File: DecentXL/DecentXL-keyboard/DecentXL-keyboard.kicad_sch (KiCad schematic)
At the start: 206 parts, among them J1 Conn_02x12_Odd_Even, J2 Conn_01x26, J3 Conn_01x04, SW0 SW_Push_45deg, SW1 SW_Push_45deg, SW2 SW_Push_45deg, SW3 SW_Push_45deg, SW4 SW_Push_45deg, SW5 SW_Push_45deg, SW6 SW_Push_45deg, SW8 SW_Push_45deg, SW9 SW_Push_45deg

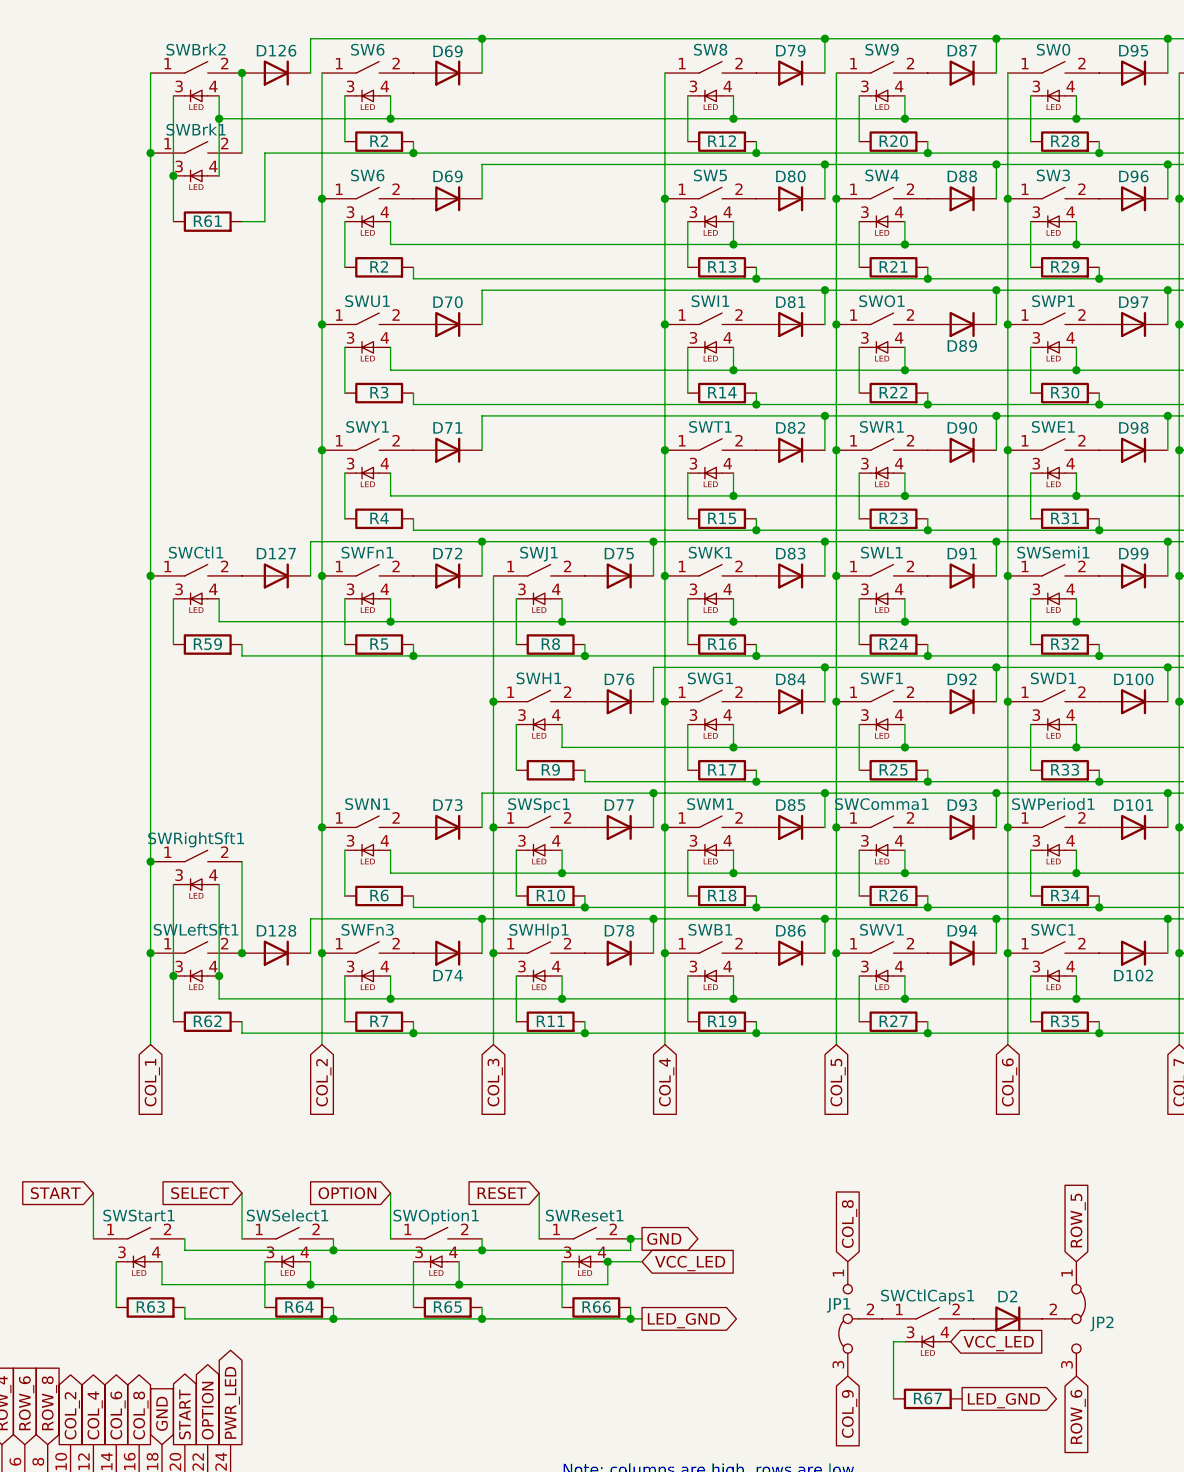
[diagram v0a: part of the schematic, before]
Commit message: DecentXL footprint library with Alps compatible footprint
Other usable footprints: MX, Kailh Choc v2
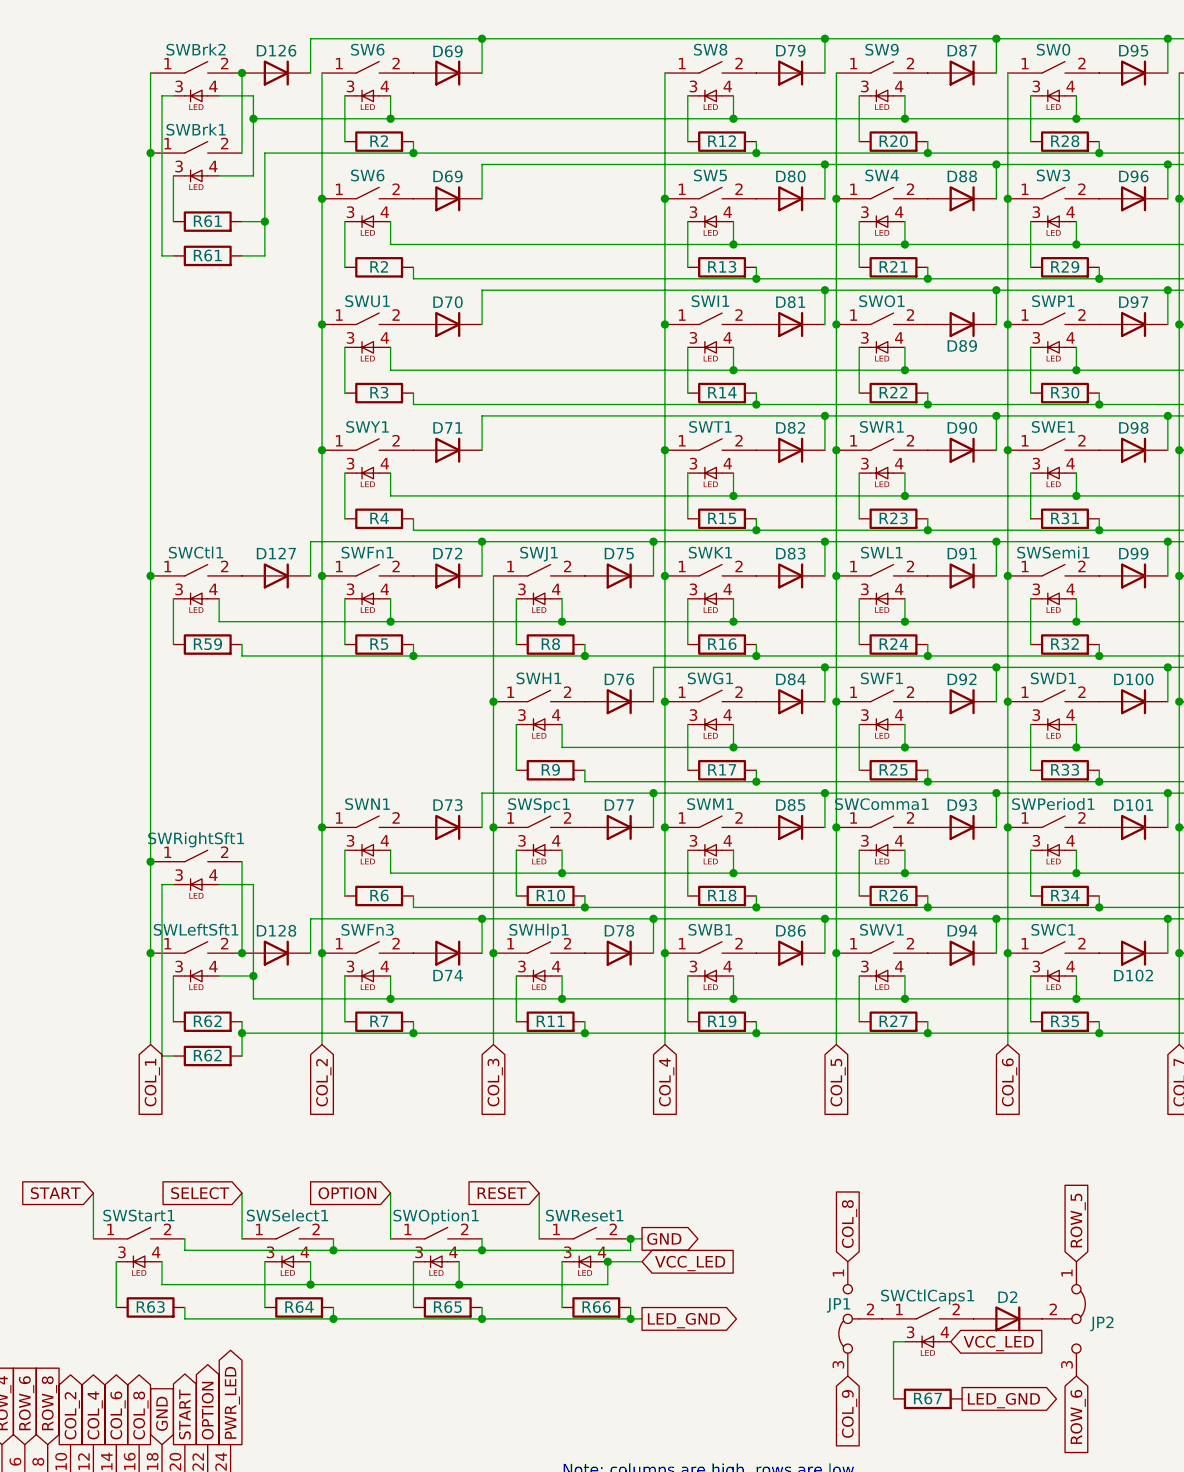
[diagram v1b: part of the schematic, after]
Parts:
- added R61, R62: R, Resistor_SMD:R_0603_1608Metric, symbol Device:R
- J1: footprint Atari130MX:IDC-Header_2x12_P2.54mm_Vertical -> Connector_IDC:IDC-Header_2x12_P2.54mm_Vertical
- SW0, SW1, SW2, SW3, SW4, SW5, SW6, SW8, SW9, SWA1, SWB1, SWBrk1, SWBrk2, SWC1, SWComma1, SWD1, SWDash1, SWDel1, SWE1, SWEqual1, SWEsc1, SWF1, SWG1, SWGT1, SWH1, SWI1, SWInv1, SWJ1, SWK1, SWL1, SWLT1, SWM1, SWN1, SWO1, SWP1, SWPeriod1, SWPlus1, SWQ1, SWR1, SWS1, SWSemi1, SWSlash1, SWStar1, SWT1, SWU1, SWV1, SWW1, SWX1, SWY1, SWZ1: footprint Atari130MX:MX-1U-LED -> DecentXL:MX-1-00U-LED
- SWCps1, SWCtl1: footprint Atari130MX:MX-1-25U-LED -> DecentXL:MX-1-25U-LED
- SWCtlCaps1, SWRightSft1: footprint Atari130MX:MX-1-75U-LED -> DecentXL:MX-1-75U-LED
- SWDel2: footprint Atari130MX:MX-2-00U -> DecentXL:MX-2-00U-LED
- SWFn1, SWFn2, SWFn3, SWFn4, SWHlp1, SWOption1, SWReset1, SWSelect1, SWStart1: footprint Atari130MX:MX-1-50U-Atari-Fn-LED -> DecentXL:MX-1-50U-Atari-Fn-LED
- SWLeftSft1: footprint Atari130MX:MX-2-25U-LED -> DecentXL:MX-2-25U-LED
- SWRet1, SWTab1: footprint Atari130MX:MX-1-50U-LED -> DecentXL:MX-1-50U-LED
- SWRet2: footprint Atari130MX:MX-ISO-RETURN -> DecentXL:MX-ISO-RETURN
- SWSpc1: footprint Atari130MX:MX-6-50U-LED -> DecentXL:MX-6-25U-LED
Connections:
- net LED_GND: now also R61.2, R62.2
- net at R62.1, SWLeftSft1.3: no longer SWRightSft1.3
- net at R61.1, SWBrk1.3: no longer SWBrk2.3
- new net: R62.1, SWRightSft1.3
- new net: R61.1, SWBrk2.3

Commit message: DecentXL PCB
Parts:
- added J4, J7: Conn_01x10, Connector_PinHeader_2.54mm:PinHeader_1x10_P2.54mm_Vertical, symbol Connector_Generic:Conn_01x10
- added J5, J6: Conn_01x10, Connector_FFC-FPC:TE_1-1734839-0_1x10-1MP_P0.5mm_Horizontal, symbol Connector_Generic:Conn_01x10
- D100, D101, D102, D103, D104, D105, D106, D107, D108, D109, D110, D111, D112, D113, D114, D115, D116, D117, D118, D119, D120, D121, D122, D123, D124, D125, D126, D127, D128, D2, D69, D70, D71, D72, D73, D74, D75, D76, D77, D78, D79, D80, D81, D82, D83, D84, D85, D86, D87, D88, D89, D90, D91, D92, D93, D94, D95, D96, D97, D98, D99: footprint Diode_SMD:D_SOD-123 -> DecentXL:D_SOD-123
- R10, R11, R12, R13, R14, R15, R16, R17, R18, R19, R2, R20, R21, R22, R23, R24, R25, R26, R27, R28, R29, R3, R30, R31, R32, R33, R34, R35, R36, R37, R38, R39, R4, R40, R41, R42, R43, R44, R45, R46, R47, R48, R49, R5, R50, R51, R52, R53, R54, R55, R56, R57, R58, R59, R6, R61, R62, R63, R64, R65, R66, R67, R7, R8, R9: footprint Resistor_SMD:R_0603_1608Metric -> DecentXL:R_0603_1608Metric
- SWBrk2: footprint DecentXL:MX-1-00U-LED -> DecentXL:MX-1-25U-LED
- SWFn1, SWFn2, SWFn3, SWFn4, SWHlp1, SWOption1, SWReset1, SWSelect1, SWStart1: footprint DecentXL:MX-1-50U-Atari-Fn-LED -> DecentXL:MX-1-00U-LED
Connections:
- net COL_1: now also JP1.3 (B)
- net COL_3: now also J6.9 (Pin_9), J7.9 (Pin_9); no longer SWHlp1.1
- net COL_8: no longer JP1.1 (A)
- net COL_9: now also JP1.1 (A); no longer JP1.3 (B)
- net GND: now also J6.8 (Pin_8), J7.8 (Pin_8); no longer D1.1 (K), SWOption1.2, SWReset1.2, SWSelect1.2, SWStart1.2
- net LED_GND: now also J6.1 (Pin_1), J7.1 (Pin_1); no longer R11.2, R63.2, R64.2, R65.2, R66.2
- net OPTION: now also J6.5 (Pin_5), J7.5 (Pin_5); no longer SWOption1.1
- net PWR_LED: now also J6.3 (Pin_3), J7.3 (Pin_3); no longer D1.2 (A)
- net RESET: now also J6.4 (Pin_4), J7.4 (Pin_4); no longer SWReset1.1
- net ROW_4: no longer D122.2 (A), SWTab1.2
- net ROW_7: no longer D117.2 (A), SWInv1.2
- net ROW_8: now also J6.10 (Pin_10), J7.10 (Pin_10); no longer D78.1 (K)
- net SELECT: now also J6.6 (Pin_6), J7.6 (Pin_6); no longer SWSelect1.1
- net START: now also J6.7 (Pin_7), J7.7 (Pin_7); no longer SWStart1.1
- net VCC_LED: now also J6.2 (Pin_2), J7.2 (Pin_2); no longer SWHlp1.4, SWOption1.4, SWReset1.4, SWSelect1.4, SWStart1.4
- new net: D122.2 (A), SWTab1.2
- new net: D117.2 (A), SWInv1.2
- new net CSL_GND: D1.1 (K), J4.3 (Pin_3), J5.3 (Pin_3), SWOption1.2, SWReset1.2, SWSelect1.2, SWStart1.2
- new net CSL_HELP: J4.2 (Pin_2), J5.2 (Pin_2), SWHlp1.1
- new net CSL_LED_GND: J4.10 (Pin_10), J5.10 (Pin_10), R11.2, R63.2, R64.2, R65.2, R66.2
- new net CSL_OPTION: J4.6 (Pin_6), J5.6 (Pin_6), SWOption1.1
- new net CSL_PWR_LED: D1.2 (A), J4.8 (Pin_8), J5.8 (Pin_8)
- new net CSL_RESET: J4.7 (Pin_7), J5.7 (Pin_7), SWReset1.1
- new net CSL_ROW_8: D78.1 (K), J4.1 (Pin_1), J5.1 (Pin_1)
- new net CSL_SELECT: J4.5 (Pin_5), J5.5 (Pin_5), SWSelect1.1
- new net CSL_START: J4.4 (Pin_4), J5.4 (Pin_4), SWStart1.1
- new net CSL_VCC_LED: J4.9 (Pin_9), J5.9 (Pin_9), SWHlp1.4, SWOption1.4, SWReset1.4, SWSelect1.4, SWStart1.4
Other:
- moved on the sheet: D1, D2, D78, J1, J2, J3, JP1, JP2, JP3, JP4, R11, R63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

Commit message: DecentXL PCB progress
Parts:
- removed JP3: SolderJumper_2_Bridged, Connector_PinHeader_2.54mm:PinHeader_1x02_P2.54mm_Horizontal, symbol Jumper:SolderJumper_2_Open
- added RV1: R_Potentiometer, DecentXL:Potentiometer_CUI-PTN06-D02CB20, symbol Device:R_Potentiometer
- J2: footprint Connector_FFC-FPC:Molex_200528-0260_1x26-1MP_P1.00mm_Horizontal -> DecentXL:Molex_200528-0260_1x26-1MP_P1.00mm_Horizontal
- JP4: footprint Connector_PinHeader_2.54mm:PinHeader_1x02_P2.54mm_Horizontal -> Jumper:SolderJumper-2_P1.3mm_Bridged_Pad1.0x1.5mm; symbol Jumper:SolderJumper_2_Open -> Jumper:SolderJumper_2_Bridged
- SWCtlCaps1: footprint DecentXL:MX-1-75U-LED -> DecentXL:MX-2-00U-LED
- SWEsc1: footprint DecentXL:MX-1-00U-LED -> DecentXL:MX-1-25U-LED
- SWTab1: footprint DecentXL:MX-1-50U-LED -> DecentXL:MX-1-75U-LED
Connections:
- net POWER: now also RV1.2
- net VCC_LED: now also RV1.1
- no-connect marks 0 -> 1
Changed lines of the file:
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@@
   (junction (at 210.82 22.86) (diameter 0) (color 0 0 0 0)
   )
+  (no_connect (at 35.56 143.51))
   (wire (pts (xy 125.73 31.75) (xy 125.73 30.48))
     (stroke (width 0) (type default))
@@
     (stroke (width 0) (type default))
   )
+  (wire (pts (xy 35.56 151.13) (xy 39.37 151.13))
+    (stroke (width 0) (type default))
+  )
   (wire (pts (xy 85.09 69.85) (xy 85.09 67.31))
     (stroke (width 0) (type default))
@@
     (stroke (width 0) (type default))
   )
-  (text "Note: columns are high, rows are low." (at 57.15 196.85 0)
+  (text "Note: columns are high, rows are low." (at 57.15 198.12 0)
     (effects (font (size 1.27 1.27)) (justify left bottom))
   )
@@
     )
   )
-  (global_label "POWER" (shape input) (at 31.75 151.13 180) (fields_autoplaced)
+  (global_label "POWER" (shape input) (at 31.75 147.32 180) (fields_autoplaced)
     (effects (font (size 1.27 1.27)) (justify right))
-    (property "Intersheetrefs" "${INTERSHEET_REFS}" (at 22.9548 151.0506 0)
+    (property "Intersheetrefs" "${INTERSHEET_REFS}" (at 22.9548 147.2406 0)
       (effects (font (size 1.27 1.27)) (justify right) hide)
     )
@@
       (effects (font (size 1.27 1.27)) hide)
     )
-    (property "Footprint" "DecentXL:MX-1-50U-LED" (at 215.9 64.77 0)
+    (property "Footprint" "DecentXL:MX-1-75U-LED" (at 215.9 64.77 0)
       (effects (font (size 1.524 1.524)) hide)
     )
@@
     )
   )
-  (symbol (lib_id "Jumper:SolderJumper_2_Open") (at 35.56 151.13 0) (unit 1)
-    (in_bom yes) (on_board yes) (dnp no) (fields_autoplaced)
-    (property "Reference" "JP3" (at 35.56 146.5412 0)
-      (effects (font (size 1.27 1.27)))
-    )
-    (property "Value" "SolderJumper_2_Bridged" (at 35.56 149.0781 0)
-      (effects (font (size 1.27 1.27)))
-    )
-    (property "Footprint" "Connector_PinHeader_2.54mm:PinHeader_1x02_P2.54mm_Horizontal" (at 35.56 151.13 0)
-      (effects (font (size 1.27 1.27)) hide)
-    )
-    (property "Datasheet" "~" (at 35.56 151.13 0)
-      (effects (font (size 1.27 1.27)) hide)
-    )
-    (pin "1")
-    (pin "2")
-    (instances
-      (project "DecentXE"
-        (path "/2f215f15-3d52-4c91-93e6-3ea03a95622f"
-          (reference "JP3") (unit 1)
-        )
-      )
-      (project "DecentXL-keyboard"
-        (path "/a9892182-6906-43e4-9038-45744b4ac951"
-          (reference "JP1") (unit 1)
-        )
-      )
-    )
-  )
   (symbol (lib_id "Jumper:Jumper_3_Bridged12") (at 83.82 161.29 270) (unit 1)
     (in_bom yes) (on_board yes) (dnp no) (fields_autoplaced)
@@
       (effects (font (size 1.27 1.27)) hide)
     )
-    (property "Footprint" "DecentXL:MX-1-75U-LED" (at 67.31 161.29 0)
+    (property "Footprint" "DecentXL:MX-2-00U-LED" (at 67.31 161.29 0)
       (effects (font (size 1.524 1.524)) hide)
     )
@@
     )
   )
-  (symbol (lib_id "Jumper:SolderJumper_2_Open") (at 35.56 158.75 0) (unit 1)
+  (symbol (lib_id "Jumper:SolderJumper_2_Bridged") (at 35.56 158.75 0) (unit 1)
     (in_bom yes) (on_board yes) (dnp no) (fields_autoplaced)
     (property "Reference" "JP4" (at 35.56 154.1612 0)
@@
       (effects (font (size 1.27 1.27)))
     )
-    (property "Footprint" "Connector_PinHeader_2.54mm:PinHeader_1x02_P2.54mm_Horizontal" (at 35.56 158.75 0)
+    (property "Footprint" "Jumper:SolderJumper-2_P1.3mm_Bridged_Pad1.0x1.5mm" (at 35.56 158.75 0)
       (effects (font (size 1.27 1.27)) hide)
     )
@@
       (effects (font (size 1.27 1.27)))
     )
-    (property "Footprint" "Connector_FFC-FPC:Molex_200528-0260_1x26-1MP_P1.00mm_Horizontal" (at 88.9 181.61 0)
+    (property "Footprint" "DecentXL:Molex_200528-0260_1x26-1MP_P1.00mm_Horizontal" (at 88.9 181.61 0)
       (effects (font (size 1.27 1.27)) hide)
     )
@@
       (effects (font (size 1.27 1.27)) hide)
     )
-    (property "Footprint" "DecentXL:MX-1-00U-LED" (at 215.9 36.83 0)
+    (property "Footprint" "DecentXL:MX-1-25U-LED" (at 215.9 36.83 0)
       (effects (font (size 1.524 1.524)) hide)
     )
@@
         )
       )
+    )
+  )
+  (symbol (lib_id "Device:R_Potentiometer") (at 35.56 147.32 180) (unit 1)
+    (in_bom yes) (on_board yes) (dnp no) (fields_autoplaced)
+    (property "Reference" "RV1" (at 37.338 146.1079 0)
+      (effects (font (size 1.27 1.27)) (justify right))
+    )
+    (property "Value" "R_Potentiometer" (at 37.338 148.5321 0)
+      (effects (font (size 1.27 1.27)) (justify right))
+    )
+    (property "Footprint" "DecentXL:Potentiometer_CUI-PTN06-D02CB20" (at 35.56 147.32 0)
+      (effects (font (size 1.27 1.27)) hide)
+    )
+    (property "Datasheet" "~" (at 35.56 147.32 0)
+      (effects (font (size 1.27 1.27)) hide)
+    )
+    (pin "1")
+    (pin "2")
+    (pin "3")
+    (instances
+      (project "DecentXL-keyboard"
+        (path "/a9892182-6906-43e4-9038-45744b4ac951"
+          (reference "RV1") (unit 1)
+        )
+      )

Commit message: DecentXL rev 1
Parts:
- removed J7: Conn_01x10, Connector_PinHeader_2.54mm:PinHeader_1x10_P2.54mm_Vertical, symbol Connector_Generic:Conn_01x10
- D1: JLC Part (none) -> C2290
- D100, D101, D102, D103, D104, D105, D106, D107, D108, D109, D110, D111, D112, D113, D114, D115, D116, D117, D118, D119, D120, D121, D122, D123, D124, D125, D126, D127, D128, D2, D69, D70, D71, D72, D73, D74, D75, D76, D77, D78, D79, D80, D81, D82, D83, D84, D85, D86, D87, D88, D89, D90, D91, D92, D93, D94, D95, D96, D97, D98, D99: JLC Part (none) -> C81598
- J1, J3, J4, RV1: now left out of the parts list
- J2: JLC Part (none) -> C60248
- J5, J6: footprint Connector_FFC-FPC:TE_1-1734839-0_1x10-1MP_P0.5mm_Horizontal -> Connector_FFC-FPC:Hirose_FH12-10S-0.5SH_1x10-1MP_P0.50mm_Horizontal; JLC Part (none) -> C709365
- R10, R11, R12, R13, R14, R15, R16, R17, R18, R19, R2, R20, R21, R22, R23, R24, R25, R26, R27, R28, R29, R3, R30, R31, R32, R33, R34, R35, R36, R37, R38, R39, R4, R40, R41, R42, R43, R44, R45, R46, R47, R48, R49, R5, R50, R51, R52, R53, R54, R55, R56, R57, R58, R59, R6, R61, R62, R63, R64, R65, R66, R67, R7, R8, R9: JLC Part (none) -> C22775
- SW0, SW1, SW2, SW3, SW4, SW5, SW6, SW8, SW9, SWA1, SWB1, SWBrk1, SWBrk2, SWC1, SWComma1, SWCps1, SWCtl1, SWCtlCaps1, SWD1, SWDash1, SWDel1, SWDel2, SWE1, SWEqual1, SWEsc1, SWF1, SWFn1, SWFn2, SWFn3, SWFn4, SWG1, SWGT1, SWH1, SWHlp1, SWI1, SWInv1, SWJ1, SWK1, SWL1, SWLT1, SWLeftSft1, SWM1, SWN1, SWO1, SWOption1, SWP1, SWPeriod1, SWPlus1, SWQ1, SWR1, SWReset1, SWRet1, SWRet2, SWRightSft1, SWS1, SWSelect1, SWSemi1, SWSlash1, SWSpc1, SWStar1, SWStart1, SWT1, SWTab1, SWU1, SWV1, SWW1, SWX1, SWY1, SWZ1: JLC Part (none) -> C193191

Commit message: DecentXL revisions
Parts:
- RV1: footprint DecentXL:Potentiometer_CUI-PTN06-D02CB20 -> Potentiometer_SMD:Potentiometer_Bourns_TC33X_Vertical
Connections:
- net COL_1: now also J1.10 (Pin_10), J2.10 (Pin_10), J3.1 (Pin_1), SW6.1, SW6.1, SWFn1.1, SWFn3.1, SWN1.1, SWU1.1, SWY1.1; no longer J1.9 (Pin_9), J2.9 (Pin_9), JP1.3 (B), SWBrk1.1, SWBrk2.1, SWCtl1.1, SWLeftSft1.1, SWRightSft1.1
- net COL_2: now also J1.11 (Pin_11), J2.11 (Pin_11), SWH1.1, SWJ1.1, SWSpc1.1; no longer J1.10 (Pin_10), J2.10 (Pin_10), J3.1 (Pin_1), SW6.1, SW6.1, SWFn1.1, SWFn3.1, SWN1.1, SWU1.1, SWY1.1
- net COL_3: now also J1.12 (Pin_12), J2.12 (Pin_12), SW5.1, SW8.1, SWB1.1, SWG1.1, SWI1.1, SWK1.1, SWM1.1, SWT1.1; no longer J1.11 (Pin_11), J2.11 (Pin_11), SWH1.1, SWJ1.1, SWSpc1.1
- net COL_4: now also J1.13 (Pin_13), J2.13 (Pin_13), SW4.1, SW9.1, SWComma1.1, SWF1.1, SWL1.1, SWO1.1, SWR1.1, SWV1.1; no longer J1.12 (Pin_12), J2.12 (Pin_12), SW5.1, SW8.1, SWB1.1, SWG1.1, SWI1.1, SWK1.1, SWM1.1, SWT1.1
- net COL_5: now also J1.14 (Pin_14), J2.14 (Pin_14), SW0.1, SW3.1, SWC1.1, SWD1.1, SWE1.1, SWP1.1, SWPeriod1.1, SWSemi1.1; no longer J1.13 (Pin_13), J2.13 (Pin_13), SW4.1, SW9.1, SWComma1.1, SWF1.1, SWL1.1, SWO1.1, SWR1.1, SWV1.1
- net COL_6: now also J1.15 (Pin_15), J2.15 (Pin_15), SW2.1, SWDash1.1, SWLT1.1, SWPlus1.1, SWS1.1, SWSlash1.1, SWW1.1, SWX1.1; no longer J1.14 (Pin_14), J2.14 (Pin_14), SW0.1, SW3.1, SWC1.1, SWD1.1, SWE1.1, SWP1.1, SWPeriod1.1, SWSemi1.1
- net COL_7: now also J1.16 (Pin_16), J2.16 (Pin_16), SW1.1, SWA1.1, SWEqual1.1, SWGT1.1, SWInv1.1, SWQ1.1, SWStar1.1, SWZ1.1; no longer J1.15 (Pin_15), J2.15 (Pin_15), SW2.1, SWDash1.1, SWLT1.1, SWPlus1.1, SWS1.1, SWSlash1.1, SWW1.1, SWX1.1
- net COL_8: now also J1.17 (Pin_17), J2.17 (Pin_17), J3.2 (Pin_2), JP1.1 (A), SWCps1.1, SWDel1.1, SWDel2.1, SWEsc1.1, SWFn2.1, SWFn4.1, SWRet1.1, SWRet2.1, SWTab1.1; no longer J1.16 (Pin_16), J2.16 (Pin_16), SW1.1, SWA1.1, SWEqual1.1, SWGT1.1, SWInv1.1, SWQ1.1, SWStar1.1, SWZ1.1
- net COL_9: now also J1.9 (Pin_9), J2.9 (Pin_9), JP1.3 (B), SWBrk1.1, SWBrk2.1, SWCtl1.1, SWLeftSft1.1, SWRightSft1.1; no longer J1.17 (Pin_17), J2.17 (Pin_17), J3.2 (Pin_2), JP1.1 (A), SWCps1.1, SWDel1.1, SWDel2.1, SWEsc1.1, SWFn2.1, SWFn4.1, SWRet1.1, SWRet2.1, SWTab1.1
